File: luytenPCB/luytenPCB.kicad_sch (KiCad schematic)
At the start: 39 parts, among them IC1 DRV8212DRLR, IC2 DRV8212DRLR, J1 Battery, J10 START_M, J11 DIST_C, J2 BDC1, J3 BDC2, J4 LINE_RF, J5 LINE_LF, J6 DIST_L, J7 DIST_LM, J8 DIST_R, J9 DIST_RM, SW1 SW_SPST, SW2 ProgSelect

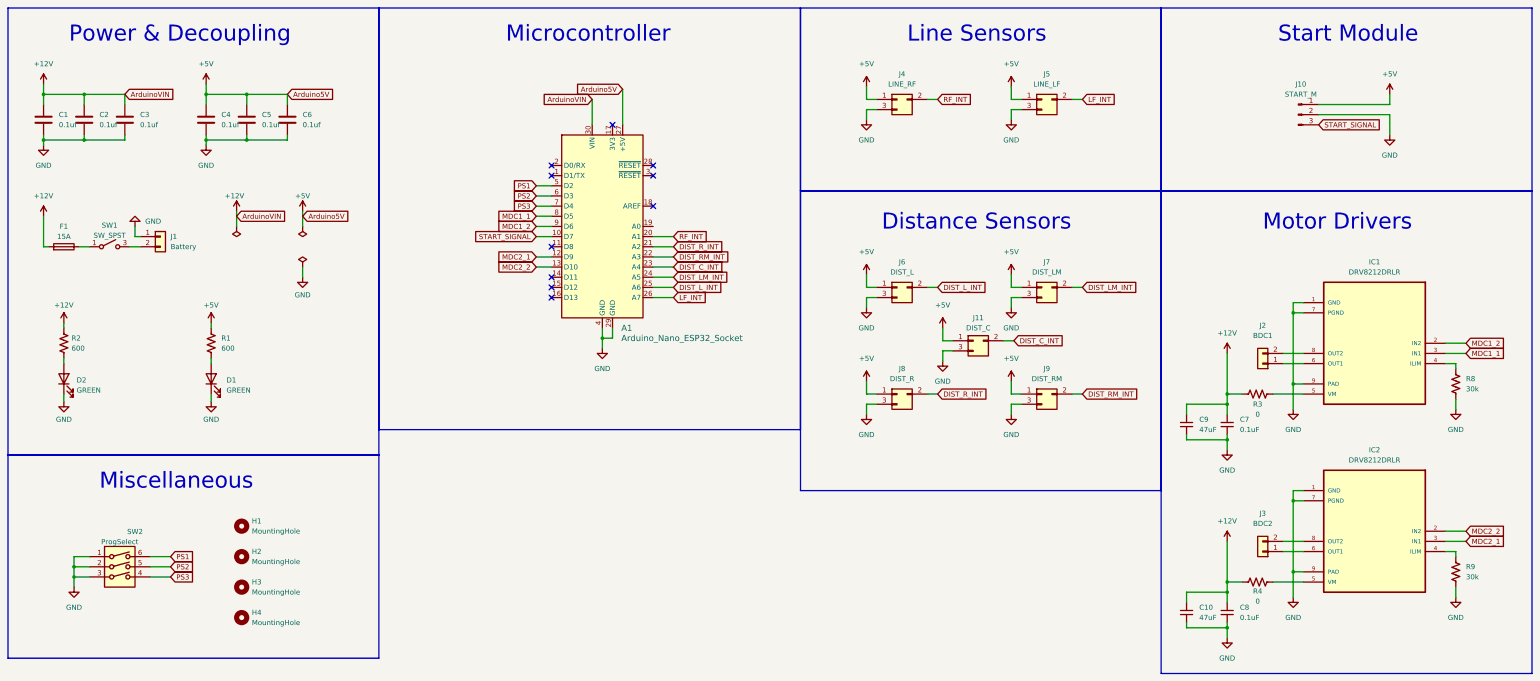
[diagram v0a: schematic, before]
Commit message: updated motor driver drv8212
changed some connections for compatibility with digital and analog dist sensors, updated optional kill switch circuit break
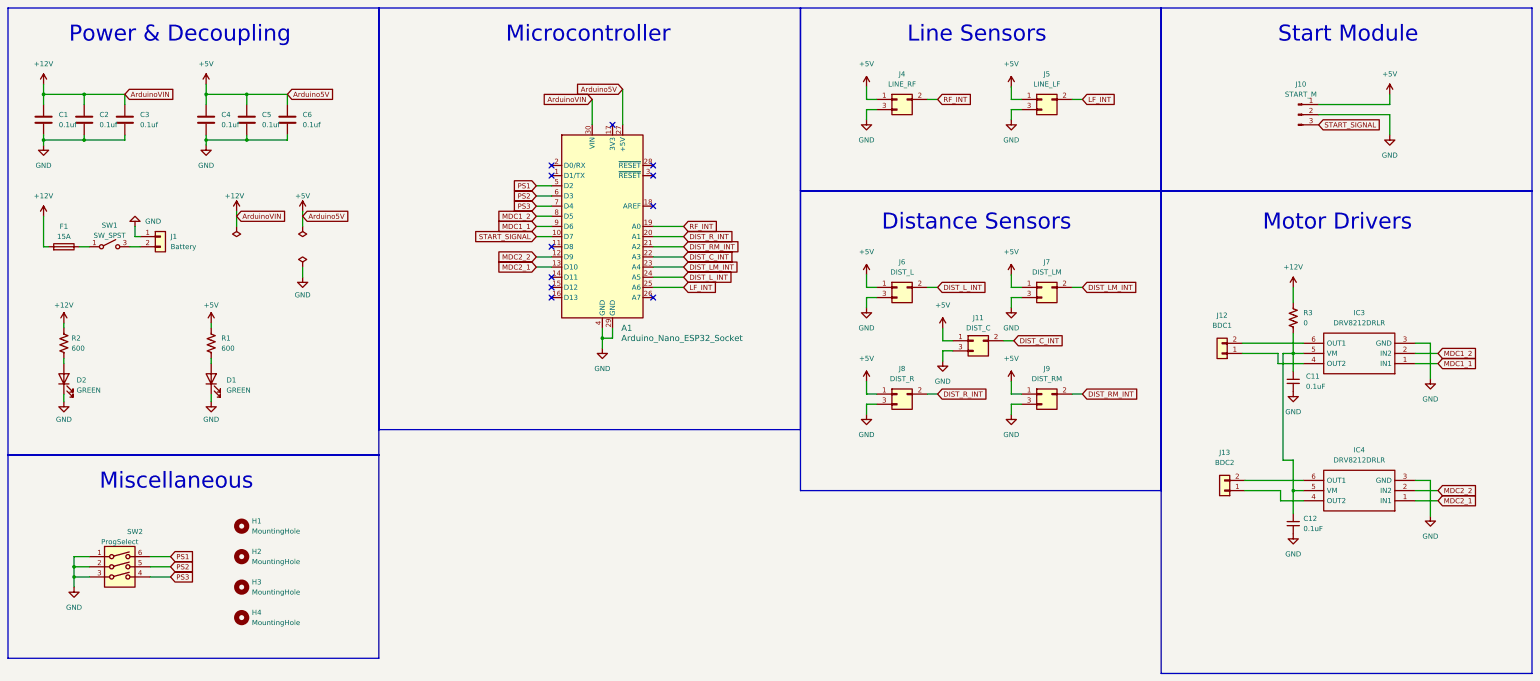
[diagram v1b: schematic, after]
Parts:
- removed C10, C9: 47uF, Capacitor_SMD:C_0805_2012Metric_Pad1.18x1.45mm_HandSolder, symbol Device:C_Small
- removed C7, C8: 0.1uF, Capacitor_SMD:C_0805_2012Metric_Pad1.18x1.45mm_HandSolder, symbol Device:C_Small
- removed IC1, IC2: DRV8212DRLR, DRV8871DDAR:VREG_LM5017MR_NOPB, symbol DRV8871DDAR:DRV8871DDAR
- removed J2: BDC1, Connector_PinHeader_2.54mm:PinHeader_1x02_P2.54mm_Vertical, symbol Connector_Generic:Conn_01x02
- removed J3: BDC2, Connector_PinHeader_2.54mm:PinHeader_1x02_P2.54mm_Vertical, symbol Connector_Generic:Conn_01x02
- removed R4: 0, Diode_SMD:D_0805_2012Metric_Pad1.15x1.40mm_HandSolder, symbol Device:R_US
- removed R8, R9: 30k, Diode_SMD:D_0805_2012Metric_Pad1.15x1.40mm_HandSolder, symbol Device:R_US
- added C11, C12: 0.1uF, Capacitor_SMD:C_0805_2012Metric_Pad1.18x1.45mm_HandSolder, symbol Device:C_Small
- added IC3, IC4: DRV8212DRLR, Package_TO_SOT_SMD:SOT-563, symbol DRV8212DRLR:DRV8212DRLR
- added J12: BDC1, Connector_PinHeader_2.54mm:PinHeader_1x02_P2.54mm_Vertical, symbol Connector_Generic:Conn_01x02
- added J13: BDC2, Connector_PinHeader_2.54mm:PinHeader_1x02_P2.54mm_Vertical, symbol Connector_Generic:Conn_01x02
- R3: footprint Diode_SMD:D_0805_2012Metric_Pad1.15x1.40mm_HandSolder -> Connector_PinHeader_2.00mm:PinHeader_1x02_P2.00mm_Vertical
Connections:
- net DIST_C_INT: now also A1.22 (A3); no longer A1.23 (A4)
- net DIST_LM_INT: now also A1.23 (A4); no longer A1.24 (A5)
- net DIST_L_INT: now also A1.24 (A5); no longer A1.25 (A6)
- net DIST_RM_INT: now also A1.21 (A2); no longer A1.22 (A3)
- net DIST_R_INT: now also A1.20 (A1); no longer A1.21 (A2)
- net GND: now also C11.2, C12.2, IC3.3 (GND), IC4.3 (GND)
- net LF_INT: now also A1.25 (A6); no longer A1.26 (A7)
- net MDC1_1: now also A1.9 (D6), IC3.1 (IN1); no longer A1.8 (D5)
- net MDC1_2: now also A1.8 (D5), IC3.2 (IN2); no longer A1.9 (D6)
- net MDC2_1: now also A1.13 (D10), IC4.1 (IN1); no longer A1.12 (D9)
- net MDC2_2: now also A1.12 (D9), IC4.2 (IN2); no longer A1.13 (D10)
- net RF_INT: now also A1.19 (A0); no longer A1.20 (A1)
- net at R3.2: now also C11.1, C12.1, IC3.5 (VM), IC4.5 (VM)
- new net: IC4.4 (OUT2), J13.1 (Pin_1)
- new net: IC4.6 (OUT1), J13.2 (Pin_2)
- new net: IC3.4 (OUT2), J12.1 (Pin_1)
- new net: IC3.6 (OUT1), J12.2 (Pin_2)
- no-connect marks 10 -> 11
